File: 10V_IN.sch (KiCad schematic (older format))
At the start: 9 parts, among them U3 LM324

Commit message: Updates, cleanup, and component association.
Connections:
- net GND: now also U3.11 (V-)
- net +10V: now reaches U3.4 (V+)
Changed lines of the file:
@@
+	1    0    0    -1
+$EndComp
+$Comp
+L power:GND #PWR0101
+U 1 1 61369EFD
+P 3000 4950
+F 0 "#PWR0101" H 3000 4700 50  0001 C CNN
+F 1 "GND" H 3005 4777 50  0000 C CNN
+F 2 "" H 3000 4950 50  0001 C CNN
+F 3 "" H 3000 4950 50  0001 C CNN
+	1    3000 4950
+	1    0    0    -1
+$EndComp
+$Comp
+L power:+10V #PWR0102
+U 1 1 6136A679
+P 3000 4350
+F 0 "#PWR0102" H 3000 4200 50  0001 C CNN
+F 1 "+10V" H 3015 4523 50  0000 C CNN
+F 2 "" H 3000 4350 50  0001 C CNN
+F 3 "" H 3000 4350 50  0001 C CNN
+	1    3000 4350
 	1    0    0    -1
 $EndComp

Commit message: Finished the schematic, except for maybe a couple test points.
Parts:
- removed U3: LM324, Package_DIP:DIP-14_W7.62mm, symbol Amplifier_Operational:LM324
- added U5: TLV9004xRUCR, Package_SO:SOIC-14_3.9x8.7mm_P1.27mm, symbol Amplifier_Operational:TLV9004xRUCR
- renumbered C15 to C24, C16 to C25, R8 to R11, R9 to R12, R10 to R13, R11 to R14, R12 to R15, R13 to R16
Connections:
- net GND: now also U5.10 (V-)
- net at R11.1, R13.2: now also U5.2 (+)
- net at R15.2: now also U5.1 (-), U5.14
- net at R12.1, R14.2: now also U5.4 (+)
- net at R16.2: now also U5.5 (-), U5.6
- new net +5V: U5.3 (V+)
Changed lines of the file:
@@
 AR Path="/60A68B69/60A952AD" Ref="R?"  Part="1"
 AR Path="/60A8EFC5/60A952AD" Ref="R?"  Part="1"
-AR Path="/60BA95F6/60A952AD" Ref="R8"  Part="1"
-F 0 "R8" V 4500 3600 50  0000 C CNN
+AR Path="/60BA95F6/60A952AD" Ref="R11"  Part="1"
+F 0 "R11" V 4500 3600 50  0000 C CNN
 F 1 "22k" V 4600 3600 50  0000 C CNN
 F 2 "Resistor_SMD:R_0805_2012Metric" V 4740 3590 50  0001 C CNN
@@
 AR Path="/60A68B69/60A98D5B" Ref="R?"  Part="1"
 AR Path="/60A8EFC5/60A98D5B" Ref="R?"  Part="1"
-AR Path="/60BA95F6/60A98D5B" Ref="R10"  Part="1"
-F 0 "R10" H 4982 3904 50  0000 R CNN
+AR Path="/60BA95F6/60A98D5B" Ref="R13"  Part="1"
+F 0 "R13" H 4982 3904 50  0000 R CNN
 F 1 "10k" H 4982 3995 50  0000 R CNN
 F 2 "Resistor_SMD:R_0805_2012Metric" V 5090 3940 50  0001 C CNN
@@
 AR Path="/60A68B69/60A9BABC" Ref="R?"  Part="1"
 AR Path="/60A8EFC5/60A9BABC" Ref="R?"  Part="1"
-AR Path="/60BA95F6/60A9BABC" Ref="R12"  Part="1"
-F 0 "R12" V 6300 3700 50  0000 C CNN
+AR Path="/60BA95F6/60A9BABC" Ref="R15"  Part="1"
+F 0 "R15" V 6300 3700 50  0000 C CNN
 F 1 "2.2k" V 6400 3700 50  0000 C CNN
 F 2 "Resistor_SMD:R_0805_2012Metric" V 6540 3690 50  0001 C CNN
@@
 $EndComp
 $Comp
-L pspice:CAP C15
+L pspice:CAP C24
 U 1 1 60A9C9D5
 P 6850 4050
-F 0 "C15" H 7028 4096 50  0000 L CNN
+F 0 "C24" H 7028 4096 50  0000 L CNN
 F 1 ".47μ" H 7028 4005 50  0000 L CNN
 F 2 "Capacitor_SMD:C_0805_2012Metric" H 6850 4050 50  0001 C CNN
@@
 AR Path="/60A68B69/61259A93" Ref="R?"  Part="1"
 AR Path="/60A8EFC5/61259A93" Ref="R?"  Part="1"
-AR Path="/60BA95F6/61259A93" Ref="R9"  Part="1"
-F 0 "R9" V 4500 5050 50  0000 C CNN
+AR Path="/60BA95F6/61259A93" Ref="R12"  Part="1"
+F 0 "R12" V 4500 5050 50  0000 C CNN
 F 1 "22k" V 4600 5050 50  0000 C CNN
 F 2 "Resistor_SMD:R_0805_2012Metric" V 4740 5040 50  0001 C CNN
@@
 AR Path="/60A68B69/61259A9F" Ref="R?"  Part="1"
 AR Path="/60A8EFC5/61259A9F" Ref="R?"  Part="1"
-AR Path="/60BA95F6/61259A9F" Ref="R11"  Part="1"
-F 0 "R11" H 4982 5354 50  0000 R CNN
+AR Path="/60BA95F6/61259A9F" Ref="R14"  Part="1"
+F 0 "R14" H 4982 5354 50  0000 R CNN
 F 1 "10k" H 4982 5445 50  0000 R CNN
 F 2 "Resistor_SMD:R_0805_2012Metric" V 5090 5390 50  0001 C CNN
@@
 AR Path="/60A68B69/61259AAD" Ref="R?"  Part="1"
 AR Path="/60A8EFC5/61259AAD" Ref="R?"  Part="1"
-AR Path="/60BA95F6/61259AAD" Ref="R13"  Part="1"
-F 0 "R13" V 6300 5150 50  0000 C CNN
+AR Path="/60BA95F6/61259AAD" Ref="R16"  Part="1"
+F 0 "R16" V 6300 5150 50  0000 C CNN
 F 1 "2.2k" V 6400 5150 50  0000 C CNN
 F 2 "Resistor_SMD:R_0805_2012Metric" V 6540 5140 50  0001 C CNN
@@
 $EndComp
 $Comp
-L pspice:CAP C16
+L pspice:CAP C25
 U 1 1 61259AB3
 P 6850 5500
-F 0 "C16" H 7028 5546 50  0000 L CNN
+F 0 "C25" H 7028 5546 50  0000 L CNN
 F 1 ".47μ" H 7028 5455 50  0000 L CNN
 F 2 "Capacitor_SMD:C_0805_2012Metric" H 6850 5500 50  0001 C CNN
@@
 	6850 5750 6700 5750
 $Comp
-L Amplifier_Operational:LM324 U3
-U 1 1 60E8554E
-P 5700 3700
-F 0 "U3" H 5700 4067 50  0000 C CNN
-F 1 "LM324" H 5700 3976 50  0000 C CNN
-F 2 "Package_DIP:DIP-14_W7.62mm" H 5650 3800 50  0001 C CNN
-F 3 "http://www.ti.com/lit/ds/symlink/lm2902-n.pdf" H 5750 3900 50  0001 C CNN
-	1    5700 3700
-	1    0    0    -1
-$EndComp
-$Comp
-L Amplifier_Operational:LM324 U3
-U 2 1 60E8746A
-P 5700 5150
-F 0 "U3" H 5700 5517 50  0000 C CNN
-F 1 "LM324" H 5700 5426 50  0000 C CNN
-F 2 "Package_DIP:DIP-14_W7.62mm" H 5650 5250 50  0001 C CNN
-F 3 "http://www.ti.com/lit/ds/symlink/lm2902-n.pdf" H 5750 5350 50  0001 C CNN
-	2    5700 5150
-	1    0    0    -1
-$EndComp
-$Comp
-L Amplifier_Operational:LM324 U3
-U 5 1 60E8F30B
-P 3100 4650
-F 0 "U3" H 3058 4696 50  0000 L CNN
-F 1 "LM324" H 3058 4605 50  0000 L CNN
-F 2 "Package_DIP:DIP-14_W7.62mm" H 3050 4750 50  0001 C CNN
-F 3 "http://www.ti.com/lit/ds/symlink/lm2902-n.pdf" H 3150 4850 50  0001 C CNN
-	5    3100 4650
-	1    0    0    -1
-$EndComp
-$Comp
-L power:GND #PWR0101
+L power:GND #PWR040
 U 1 1 61369EFD
 P 3000 4950
-F 0 "#PWR0101" H 3000 4700 50  0001 C CNN
+F 0 "#PWR040" H 3000 4700 50  0001 C CNN
 F 1 "GND" H 3005 4777 50  0000 C CNN
 F 2 "" H 3000 4950 50  0001 C CNN
@@
 $EndComp
 $Comp
-L power:+10V #PWR0102
-U 1 1 6136A679
+L power:+5V #PWR039
+U 1 1 6197FF17
 P 3000 4350
-F 0 "#PWR0102" H 3000 4200 50  0001 C CNN
-F 1 "+10V" H 3015 4523 50  0000 C CNN
+F 0 "#PWR039" H 3000 4200 50  0001 C CNN
+F 1 "+5V" H 3015 4523 50  0000 C CNN
 F 2 "" H 3000 4350 50  0001 C CNN
 F 3 "" H 3000 4350 50  0001 C CNN
@@
 	1    0    0    -1
 $EndComp
+$Comp
+L Amplifier_Operational:TLV9004xRUCR U5
+U 1 1 61E50AE5
+P 5700 3700
+F 0 "U5" H 5700 4067 50  0000 C CNN
+F 1 "TLV9004xRUCR" H 5700 3976 50  0000 C CNN
+F 2 "Package_SO:SOIC-14_3.9x8.7mm_P1.27mm" H 5700 3700 50  0001 C CNN
+F 3 "http://www.ti.com/lit/ds/symlink/tlv9004.pdf" H 5750 3900 50  0001 C CNN
+	1    5700 3700
+	1    0    0    -1
+$EndComp
+$Comp
+L Amplifier_Operational:TLV9004xRUCR U5
+U 2 1 61E51335
+P 5700 5150
+F 0 "U5" H 5700 5517 50  0000 C CNN
+F 1 "TLV9004xRUCR" H 5700 5426 50  0000 C CNN
+F 2 "Package_SO:SOIC-14_3.9x8.7mm_P1.27mm" H 5700 5150 50  0001 C CNN
+F 3 "http://www.ti.com/lit/ds/symlink/tlv9004.pdf" H 5750 5350 50  0001 C CNN
+	2    5700 5150
+	1    0    0    -1
+$EndComp
+$Comp
+L Amplifier_Operational:TLV9004xRUCR U5
+U 5 1 61E51DBB
+P 3100 4650
+F 0 "U5" H 3058 4696 50  0000 L CNN
+F 1 "TLV9004xRUCR" H 3058 4605 50  0000 L CNN
+F 2 "Package_SO:SOIC-14_3.9x8.7mm_P1.27mm" H 3100 4650 50  0001 C CNN
+F 3 "http://www.ti.com/lit/ds/symlink/tlv9004.pdf" H 3150 4850 50  0001 C CNN
+	5    3100 4650
+	1    0    0    -1
+$EndComp

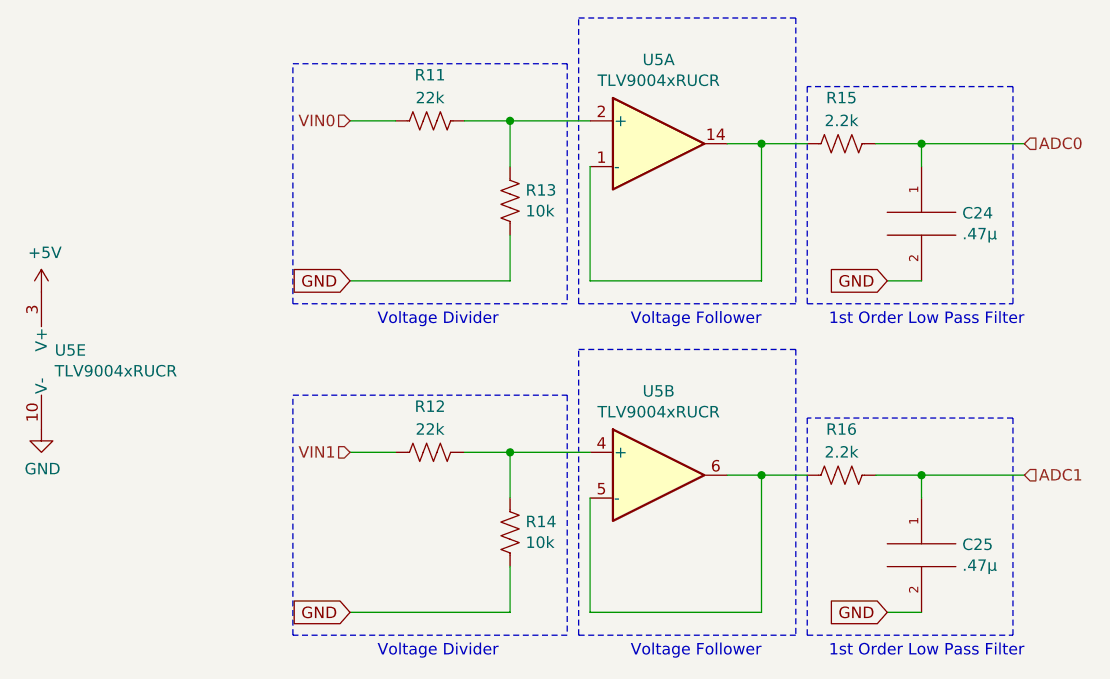
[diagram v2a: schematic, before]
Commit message: Routed ADC inputs and adjusted some trace widths
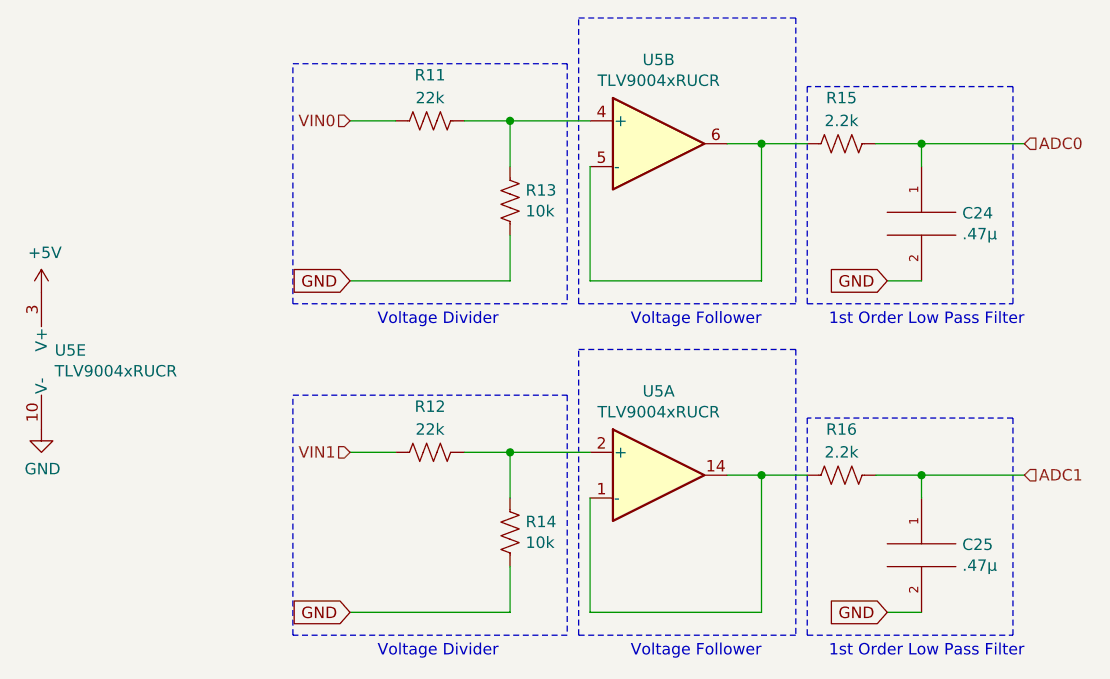
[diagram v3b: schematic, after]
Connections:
- net at R11.1, R13.2: now also U5.4 (+); no longer U5.2 (+)
- net at U5.1 (-), U5.14: now also R16.2; no longer R15.2
- net at R12.1, R14.2: now also U5.2 (+); no longer U5.4 (+)
- net at U5.5 (-), U5.6: now also R15.2; no longer R16.2
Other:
- moved on the sheet: U5A, U5B
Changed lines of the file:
@@
 L Amplifier_Operational:TLV9004xRUCR U5
 U 1 1 61E50AE5
+P 5700 5150
+F 0 "U5" H 5700 5517 50  0000 C CNN
+F 1 "TLV9004xRUCR" H 5700 5426 50  0000 C CNN
+F 2 "Package_SO:SOIC-14_3.9x8.7mm_P1.27mm" H 5700 5150 50  0001 C CNN
+F 3 "http://www.ti.com/lit/ds/symlink/tlv9004.pdf" H 5750 5350 50  0001 C CNN
+	1    5700 5150
+	1    0    0    -1
+$EndComp
+$Comp
+L Amplifier_Operational:TLV9004xRUCR U5
+U 2 1 61E51335
 P 5700 3700
 F 0 "U5" H 5700 4067 50  0000 C CNN
@@
 F 2 "Package_SO:SOIC-14_3.9x8.7mm_P1.27mm" H 5700 3700 50  0001 C CNN
 F 3 "http://www.ti.com/lit/ds/symlink/tlv9004.pdf" H 5750 3900 50  0001 C CNN
-	1    5700 3700
+	2    5700 3700
 	1    0    0    -1
 $EndComp
-$Comp
-L Amplifier_Operational:TLV9004xRUCR U5
-U 2 1 61E51335
-P 5700 5150
-F 0 "U5" H 5700 5517 50  0000 C CNN
-F 1 "TLV9004xRUCR" H 5700 5426 50  0000 C CNN
-F 2 "Package_SO:SOIC-14_3.9x8.7mm_P1.27mm" H 5700 5150 50  0001 C CNN
-F 3 "http://www.ti.com/lit/ds/symlink/tlv9004.pdf" H 5750 5350 50  0001 C CNN
-	2    5700 5150
-	1    0    0    -1
-$EndComp
